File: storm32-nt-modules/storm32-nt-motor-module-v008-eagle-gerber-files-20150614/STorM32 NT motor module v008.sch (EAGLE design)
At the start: 12 parts, among them IC1 MPU6050

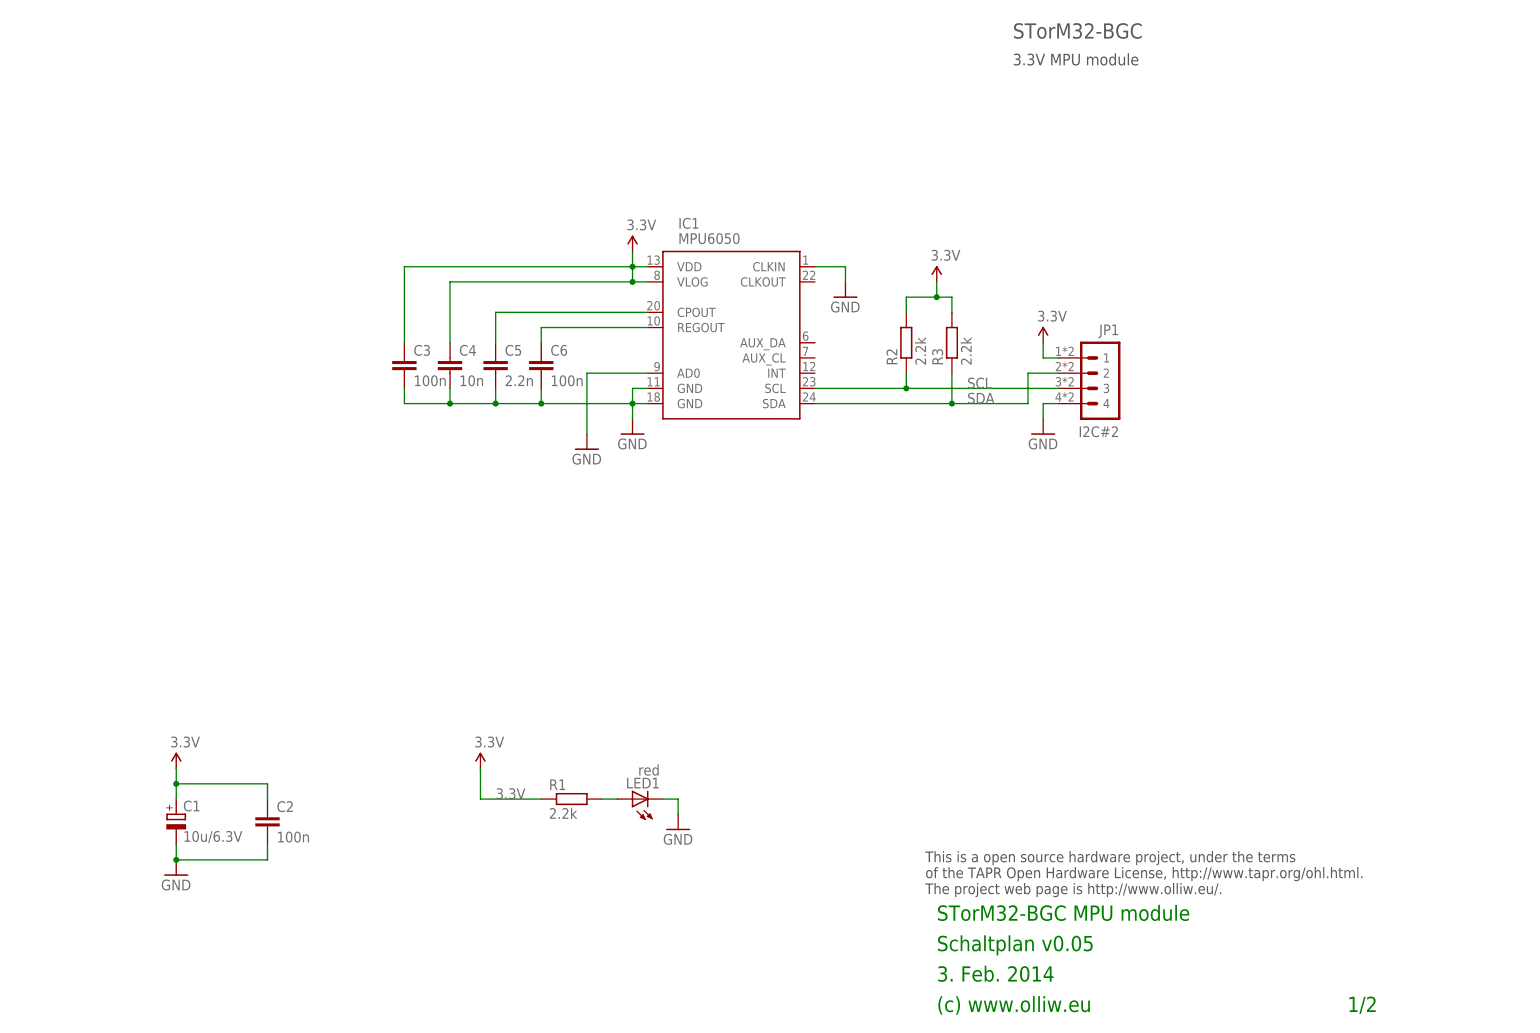
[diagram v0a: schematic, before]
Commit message: storm32-nt motor&mpu module files uploaded
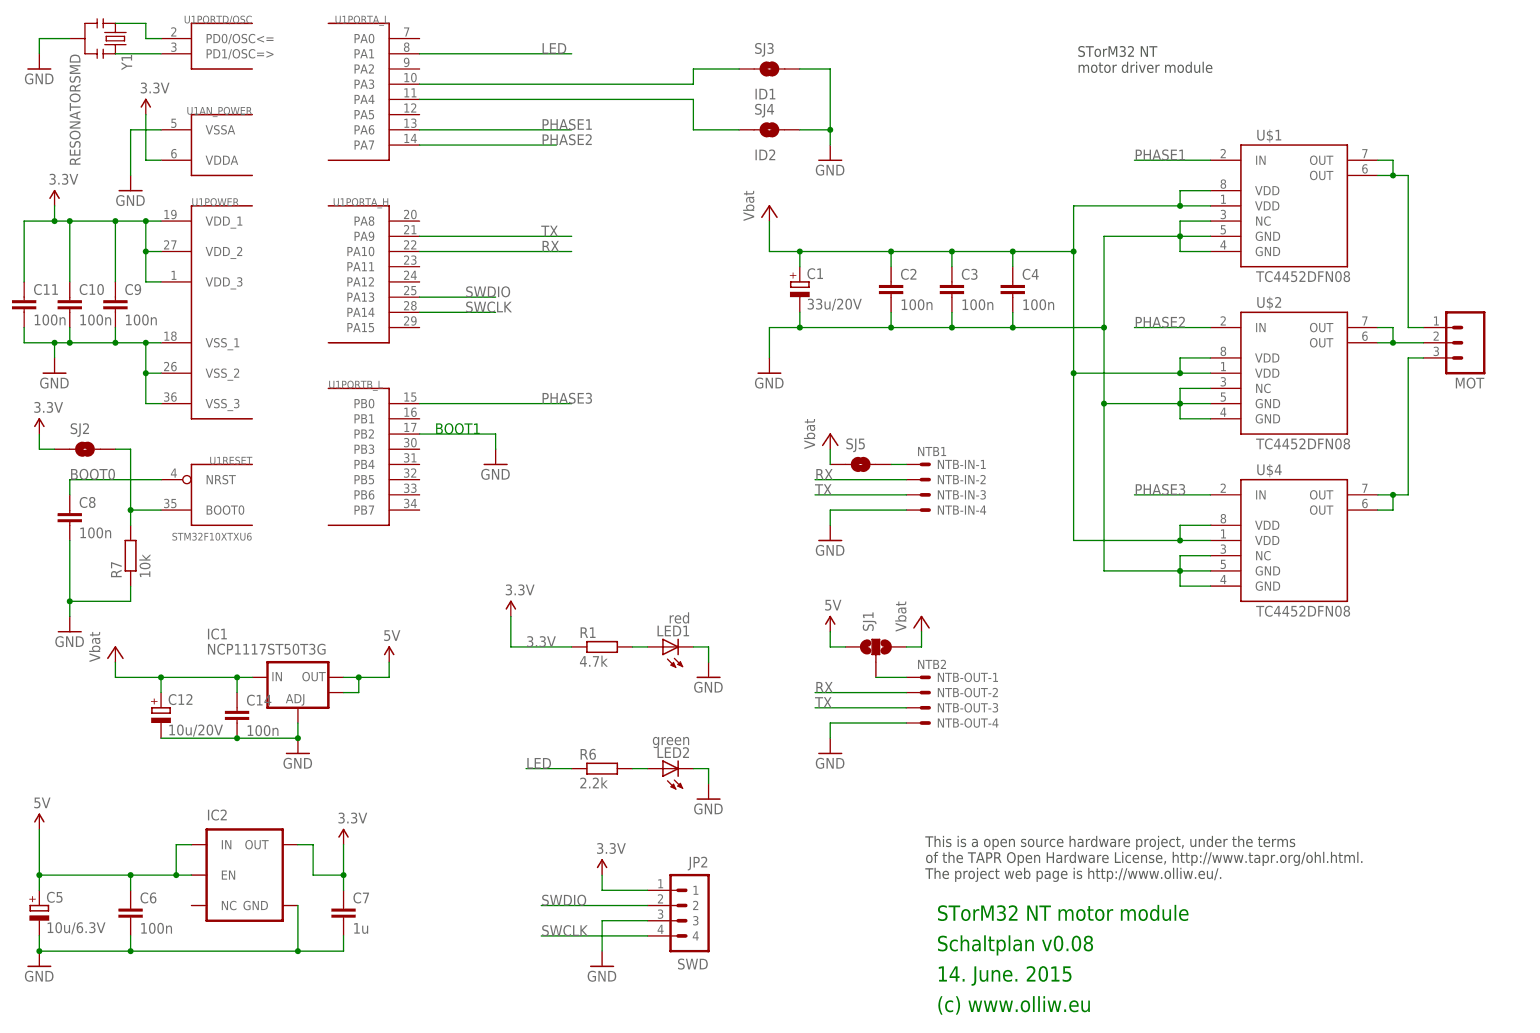
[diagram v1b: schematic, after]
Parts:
- removed JP1: I2C#2, # stdlib:P4X1_1P27MOLEX-BOTH
- removed R2, R3: 2.2k, rcl:R-EU_R0603
- added C10, C11, C14, C8, C9: 100n, rcl:C-EUC0603
- added C12: 10u/20V, rcl:CPOL-EUSMCB
- added C7: 1u, rcl:C-EUC0603
- added IC2: (no value), # SparkFun2:V_REG_TPS76433SOT23-5
- added JP2: SWD, # stdlib:P4X1_1P27-OCT_BILEX
- added LED2: green, led:LEDCHIPLED_0603
- added MOT: (no value), # SparkFun:M03PTH
- added NTB-IN: NTB1, con-jst2:SM04B-SRSS-TB
- added NTB-OUT: NTB2, con-jst2:SM04B-SRSS-TB
- added R6: 2.2k, rcl:R-EU_R0603
- added R7: 10k, rcl:R-EU_R0603
- added SJ1: (no value), # SparkFun2:SOLDERJUMPER_2WAYT
- added SJ2: BOOT0, # SparkFun2:SOLDERJUMPERNO
- added SJ3: ID1, # SparkFun2:SOLDERJUMPERNO
- added SJ4: ID2, # SparkFun2:SOLDERJUMPERNO
- added SJ5: SOLDERJUMPER, # SparkFun2:SOLDERJUMPER
- added U$1, U$2, U$4: TC4452DFN08, # stdlib:TC4452DFN08
- added U1: STM32F10XTXU6, # stm32:STM32F10XTXU6
- added Y1: RESONATORSMD, # SparkFun2:RESONATORSMD
- C1: value 10u/6.3V -> 33u/20V; device rcl:CPOL-EUSMCB -> rcl:CPOL-EUSMCC
- C4: value 10n -> 100n
- C5: value 2.2n -> 10u/6.3V; device rcl:C-EUC0603 -> rcl:CPOL-EUSMCB
- IC1: value MPU6050 -> NCP1117ST50T3G; device # SparkFun2:IMU3000 -> # SparkFun2:V_REG_LM1117SOT223
- R1: value 2.2k -> 4.7k
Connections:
- removed net N$20: C6.1, IC1.REGOUT
- removed net N$24: C5.1, IC1.CPOUT
- removed net SCL: IC1.SCL, JP1.3, R2.1
- removed net SDA: IC1.SDA, JP1.2, R3.1
- new net 5V: C5.+, C6.1, IC1.OUT, IC1.OUT@1, IC2.EN, IC2.IN, SJ1.1
- new net LED: R6.1, U1PORTA_L.PA1
- new net N$1: MOT.2, U$2.OUT, U$2.OUT@2
- new net N$10: U1PORTD/OSC.PD1/OSC=>, Y1.3
- new net N$12: LED2.A, R6.2
- new net N$13: NTB-IN-1.S, SJ5.2
- new net N$2: NTB-OUT-1.S, SJ1.2
- new net N$3: SJ3.1, U1PORTA_L.PA3
- new net N$4: SJ4.1, U1PORTA_L.PA4
- new net N$5: MOT.1, U$1.OUT, U$1.OUT@2
- new net N$6: MOT.3, U$4.OUT, U$4.OUT@2
- new net N$7: C8.1, U1RESET.NRST
- new net N$8: R7.2, SJ2.2, U1RESET.BOOT0
- new net N$9: U1PORTD/OSC.PD0/OSC<=, Y1.1
- new net PHASE1: U$1.IN, U1PORTA_L.PA6
- new net PHASE2: U$2.IN, U1PORTA_L.PA7
- new net PHASE3: U$4.IN, U1PORTB_L.PB0
- new net RX: NTB-IN-2.S, NTB-OUT-2.S, U1PORTA_H.PA10
- new net SWCLK: JP2.4, U1PORTA_H.PA14
- new net SWDIO: JP2.2, U1PORTA_H.PA13
- new net TX: NTB-IN-3.S, NTB-OUT-3.S, U1PORTA_H.PA9
- new net VBAT: C1.+, C12.+, C14.1, C2.1, C3.1, C4.1, IC1.IN, SJ1.3, SJ5.1, U$1.VDD, U$1.VDD@2, U$2.VDD, U$2.VDD@2, U$4.VDD, U$4.VDD@2
- net 3.3V: now also C10.1, C11.1, C7.1, C9.1, IC2.OUT, JP2.1, SJ2.1, U1AN_POWER.VDDA, U1POWER.VDD_1, U1POWER.VDD_2, U1POWER.VDD_3; no longer C1.+, C2.1, C3.1, C4.1, IC1.VDD, IC1.VLOG, JP1.1, R2.2, R3.2
- net GND: now also C10.2, C11.2, C12.-, C14.2, C5.-, C7.2, C8.2, C9.2, IC1.ADJ, IC2.GND, JP2.3, LED2.C, NTB-IN-4.S, NTB-OUT-4.S, R7.1, SJ3.2, SJ4.2, U$1.GND, U$1.GND@2, U$1.NC, U$2.GND, U$2.GND@2, U$2.NC, U$4.GND, U$4.GND@2, U$4.NC, U1AN_POWER.VSSA, U1PORTB_L.PB2, U1POWER.VSS_1, U1POWER.VSS_2, U1POWER.VSS_3, Y1.2; no longer C5.2, IC1.AD0, IC1.CLKIN, IC1.GND@11, IC1.GND@18, JP1.4
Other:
- note added: "14. June. 2015"
- note added: "BOOT1"
- note added: "STorM32 NT motor driver module"
- note added: "STorM32 NT motor module"
- note added: "Schaltplan v0.08"
- note removed: "1/2"
- note removed: "3. Feb. 2014"
- note removed: "3.3V MPU module"
- note removed: "STorM32-BGC"
- note removed: "STorM32-BGC MPU module"
- note removed: "Schaltplan v0.05"
- moved on the sheet: C1, C2, C3, C4, C6, LED1, R1
